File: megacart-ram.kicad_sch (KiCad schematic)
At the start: 29 parts, among them J1 Conn_02x08_Counter_Clockwise, U1 AS6C4008-55PCN, U10 7432, U11 7432, U12 74LS138, U13 74HC273, U2 HM62256BLP, U3 74HC74, U4 7421, U5 7421, U6 7402, U7 74HC04, U8 7408, U9 7408

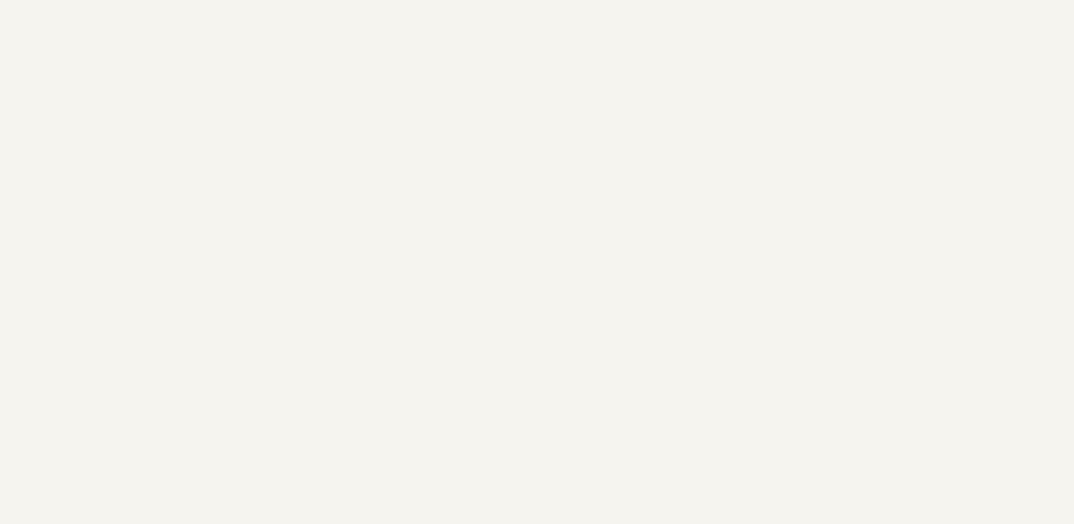
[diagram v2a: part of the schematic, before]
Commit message: Add explicit power units for 7400 ICs.
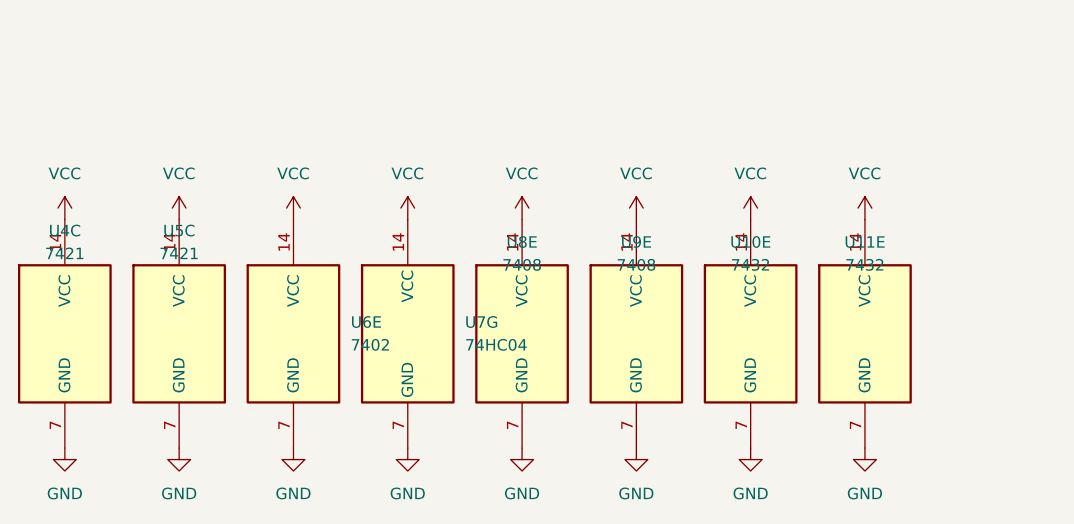
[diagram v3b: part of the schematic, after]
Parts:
- added unit 5 of U10
- added unit 5 of U11
- added unit 3 of U4
- added unit 3 of U5
- added unit 5 of U6
- added unit 7 of U7
- added unit 5 of U8
- added unit 5 of U9
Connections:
- net GND: now also U10.7 (GND), U11.7 (GND), U4.7 (GND), U5.7 (GND), U6.7 (GND), U7.7 (GND), U8.7 (GND), U9.7 (GND)
- net VCC: now also U10.14 (VCC), U11.14 (VCC), U4.14 (VCC), U5.14 (VCC), U6.14 (VCC), U7.14 (VCC), U8.14 (VCC), U9.14 (VCC)

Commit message: First pass at routing PCB.
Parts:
- removed C4, C5, C8: C, Capacitor_THT:C_Disc_D5.0mm_W2.5mm_P2.50mm, symbol Device:C
- added unit 4 of U11
- added unit 3 of U3
- J1: symbol Connector_Generic:Conn_02x08_Counter_Clockwise -> Connector_Generic:Conn_02x08_Odd_Even
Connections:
- net GND: now also U11.12, U11.13, U3.7 (GND)
- net VCC: now also U3.14 (VCC)
- net at J1.10 (Pin_10), J1.12 (Pin_12), J1.14 (Pin_14)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: now also J1.2 (Pin_2), J1.4 (Pin_4), J1.6 (Pin_6), J1.8 (Pin_8); no longer J1.11 (Pin_11), J1.13 (Pin_13), J1.15 (Pin_15), J1.9 (Pin_9)
- net at U12.10 (O5): now also J1.11 (Pin_11); no longer J1.6 (Pin_6)
- net at U12.11 (O4): now also J1.9 (Pin_9); no longer J1.5 (Pin_5)
- net at U12.12 (O3): now also J1.7 (Pin_7); no longer J1.4 (Pin_4)
- net at U12.13 (O2): now also J1.5 (Pin_5); no longer J1.3 (Pin_3)
- net at U12.14 (O1): now also J1.3 (Pin_3); no longer J1.2 (Pin_2)
- net at U12.7 (O7): now also J1.15 (Pin_15); no longer J1.8 (Pin_8)
- net at U12.9 (O6): now also J1.13 (Pin_13); no longer J1.7 (Pin_7)
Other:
- moved on the sheet: C1, C10, C11, C12, C13, C2, C3, C6, C7, C9

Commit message: Finalize PCB design.
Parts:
- added C4, C5, C8: C, Capacitor_THT:C_Disc_D5.0mm_W2.5mm_P2.50mm, symbol Device:C
- U10, U11: value 7432 -> 74HCT32
- U12: value 74LS138 -> 74HCT138
- U13: value 74HC273 -> 74HCT273
- U2: value HM62256BLP -> AS6C62256-55PCN
- U3: value 74HC74 -> 74HCT74
- U4, U5: value 7421 -> 74HCT21
- U6: value 7402 -> 74HCT02
- U7: value 74HC04 -> 74HCT04
- U8, U9: value 7408 -> 74HCT08
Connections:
- net GND: now also C4.2, C5.2, C8.2
- net VCC: now also C4.1, C5.1, C8.1
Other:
- moved on the sheet: C10, C11, C12, C13, C6, C7, C9

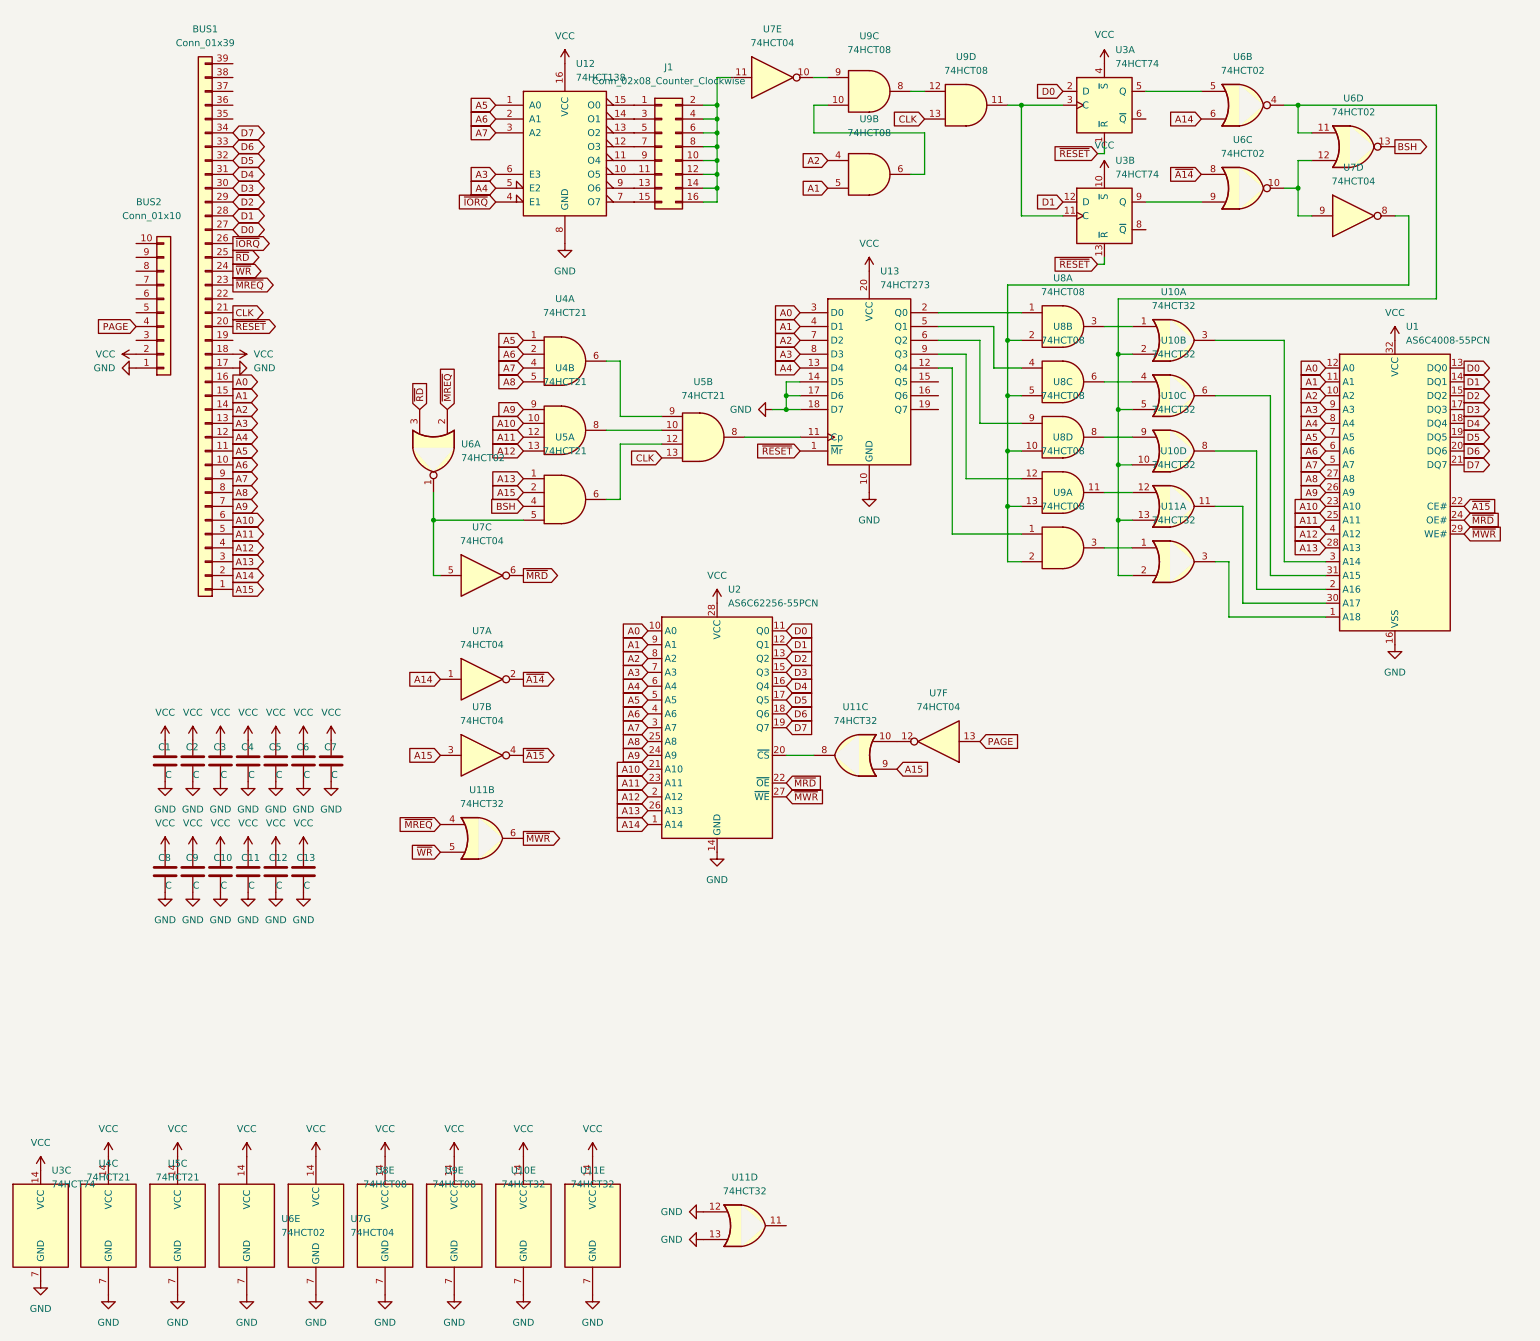
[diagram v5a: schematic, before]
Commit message: Updated revision of PCB supporting bank mirroring for 64/128/256K MegaCarts.
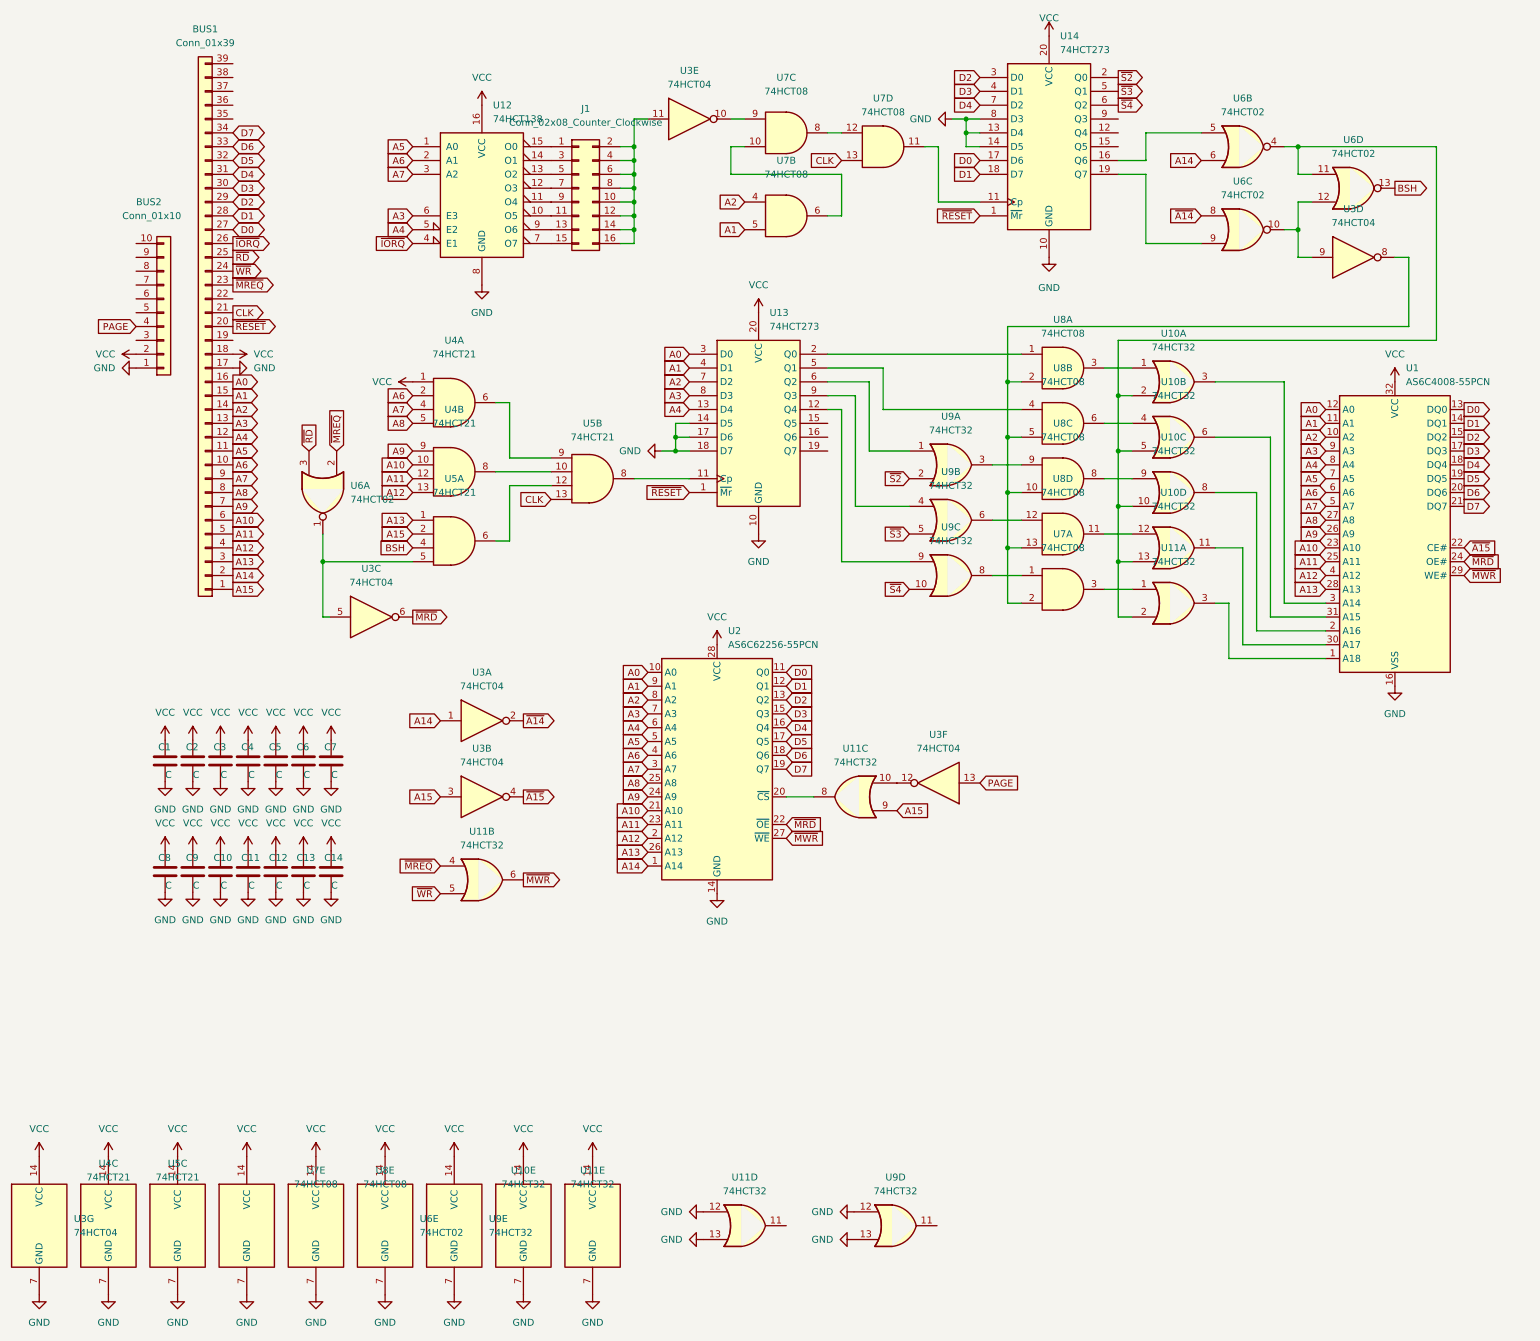
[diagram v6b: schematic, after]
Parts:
- removed U3: 74HCT74, Package_DIP:DIP-14_W7.62mm, symbol 74xx:74HC74
- removed unit 7 of U7
- added C14: C, Capacitor_THT:C_Disc_D5.0mm_W2.5mm_P2.50mm, symbol Device:C
- added U14: 74HCT273, Package_DIP:DIP-20_W7.62mm, symbol 74xx:74HC273
- added unit 7 of U3
- added U9: 74HCT32, Package_DIP:DIP-14_W7.62mm, symbol 74xx:74LS32
- renumbered U7 to U3, U9 to U7
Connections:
- net A5: no longer U4.1
- net D0: now also U14.17 (D6)
- net D1: now also U14.18 (D7)
- net D2: now also U14.3 (D0)
- net D3: now also U14.4 (D1)
- net D4: now also U14.7 (D2)
- net GND: now also C14.2, U14.10 (GND), U14.13 (D4), U14.14 (D5), U14.8 (D3), U3.7 (GND), U9.12, U9.13, U9.7 (GND)
- net VCC: now also U4.1, C14.1, U14.20 (VCC), U3.14 (VCC), U9.14 (VCC)
- net ~{RESET}: now also U14.1 (~{Mr})
- net at U6.5: now also U14.16 (Q6)
- net at U13.12 (Q4): now also U9.9; no longer U7.1
- net at U13.6 (Q2): now also U9.1; no longer U8.9
- net at U13.9 (Q3): now also U9.4; no longer U8.12
- net at U7.11: now also U14.11 (Cp)
- net at U6.9: now also U14.19 (Q7)
- new net: U8.12, U9.6
- new net: U8.9, U9.3
- new net: U7.1, U9.8
- new net ~{S2}: U14.2 (Q0), U9.2
- new net ~{S3}: U14.5 (Q1), U9.5
- new net ~{S4}: U14.6 (Q2), U9.10
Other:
- moved on the sheet: J1, U1, U10A, U10B, U10C, U10D, U11A, U11B, U11C, U12, U13, U2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

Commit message: Renumber some components.
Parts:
- renumbered C2 to C1, C6 to C12, C3 to C13, C12 to C14, C1 to C2, C13 to C3, C14 to C4, C4 to C5, C5 to C6, U2 to U1, U6 to U12, U3 to U13, U12 to U14, U1 to U2, U13 to U3, U14 to U4, U4 to U5, U5 to U6
